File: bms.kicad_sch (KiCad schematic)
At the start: 3 parts

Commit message: buckboost: draft LM5176 4-switch power stage
Placed and wired the LM5176 (U1, HTSSOP-28-EP, LCSC C442493 per
TOPOLOGY.md) plus its support network:

Power stage: Q1..Q4 (30V/20A N-FET placeholder -- v1's FDS9926A is
undersized for v2's 5A/6.5A-peak spec, so this is marked TBD for a
proper JLCPCB Basic pick), L1 6.8uH, R8 5m current sense, boot caps
C5/C6 100nF, output caps C10/C11 22uF each.

Chip support: VIN caps C1/C2 22uF, VCC decoupling C3 2.2uF, BIAS C4
1uF, feedback R1/R2 (110k/10k -> 12.0V from LM5176's 1.0V Vref),
COMP R3 20k + C8 4.7nF, SS C7 10nF, RT R4 40.2k (~500kHz), EN
pull-up R6 100k to BAT+. MODE and DITH tied to GND.

Named nets wired: BAT+, GND, VOUT_12V, SW1, SW2, HDRV1/2, LDRV1/2,
BOOT1/2, FB, LM5176_VCC, LM5176_BIAS, SS, COMP, COMP_MID, RT, EN.
No hierarchical sheet pins -- power rails cross sheets via global
labels per the root-sheet plan.

TBD annotation on-sheet lists what needs a review pass: FET MPN,
CS/CSG hookup (currently unconnected -- either wire R8 across L1 as
high-side inductor sense OR switch to Rds(on) sensing on Q2/Q3),
SLOPE resistor R5 sizing, and optional PGOOD LED.

Also cleaned the three TEMPLATE_R/C/D placeholder symbols that
create_schematic left in all four sub-sheets.

Co-Authored-By: Claude Opus 4.7 <noreply@anthropic.com>
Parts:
- removed _TEMPLATE_C: C_TEMPLATE, symbol Device:C
- removed _TEMPLATE_D: LED_TEMPLATE, symbol Device:LED
- removed _TEMPLATE_R: R_TEMPLATE, symbol Device:R

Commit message: bms: draft the BQ76920 + cell holder + FET stack + protection sheet
27 components, 21 nets, ERC clean apart from cross-sheet BAT+/GND
globals that resolve once charger + input sheets land. Same
architecture as v1: BAT- (pre-Rsns) → R9 (5 mΩ shunt) → BQ76920
VSS+SRN + Q1(DSG).S; Q1.D + Q2.D = MID; Q2.S = system GND. Q1/Q2 are
30V/20A_NFET placeholders — pick the same MPN as the buckboost stack
when parts lock.

v2 additions vs v1: 15V TVS on VC1/VC2/VC3 cell-sense lines
(D1/D2/D3), 100nF differential cell-sense caps (v1 used 1nF —
smaller than TI EVM recommends), 5-pin I²C+ALERT breakout header.

Placement is on the sparse side (~245×155 mm sheet fill) because the
new autoplace_schematic recipe over-spreads at these compact params.
NOTES.md documents the wrap-then-restore pattern the workflow needed:
autoplace → verify the apply/rewire actually landed on disk → re-wire
by hand if not (which was the case here — apply reported success but
the file came back empty of labels/wires). Task #61 tracks the fix.

NOTES.md also captures the compact_v3 tuning + the autoplace_schematic
tool caveats so the next session doesn't retrace them.

Co-Authored-By: Claude Opus 4.7 <noreply@anthropic.com>
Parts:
- added BAT1: 3× 18650, symbol power_module_lib:BH-18650-B5BA016
- added C1, C2, C3, C4, C6: 100nF, Capacitor_SMD:C_0603_1608Metric, symbol Device:C
- added C5, C7: 1uF, Capacitor_SMD:C_0603_1608Metric, symbol Device:C
- added D1, D2, D3: SMAJ15A, Diode_SMD:D_SMA, symbol Device:D_TVS
- added J1: I2C+ALERT, Connector_PinHeader_2.54mm:PinHeader_1x05_P2.54mm_Vertical, symbol Connector_Generic:Conn_01x05
- added Q1, Q2: 30V/20A_NFET, Package_TO_SOT_SMD:SOIC-8_3.9x4.9mm_P1.27mm, symbol Device:Q_NMOS
- added R1, R10, R11, R2, R3, R4: 100, Resistor_SMD:R_0603_1608Metric, symbol Device:R
- added R5, R6, R7, R8: 10k, Resistor_SMD:R_0603_1608Metric, symbol Device:R
- added R9: 5m, Resistor_SMD:R_2512_6332Metric, symbol Device:R
- added TH1: 10k NTC (103AT), Resistor_SMD:R_0603_1608Metric, symbol Device:Thermistor_NTC
- added U1: BQ7692003, Package_SO:TSSOP-20_4.4x6.5mm_P0.65mm, symbol Battery_Management:BQ76920PW
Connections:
- new net ALERT: J1.5 (Pin_5), R7.2, U1.20 (ALERT)
- new net BAT+: BAT1.1, C6.1, R4.2, U1.10 (BAT), U1.9 (REGSRC)
- new net BAT-: BAT1.6, R1.2, R9.1, U1.18 (SRP)
- new net CAP1: C7.1, U1.7 (CAP1)
- new net CELL1_TOP: BAT1.4, BAT1.5, R2.2
- new net CELL2_TOP: BAT1.2, BAT1.3, R3.2
- new net CHG_DRV: R11.1, U1.2 (CHG)
- new net DSG_DRV: R10.1, U1.1 (DSG)
- new net GND: Q2.S
- new net MID: Q1.D, Q2.D
- new net Q1_G: Q1.G, R10.2
- new net Q2_G: Q2.G, R11.2
- new net REGOUT: C5.1, J1.1 (Pin_1), R5.1, R6.1, R7.1, R8.1, U1.8 (REGOUT)
- new net SCL: J1.4 (Pin_4), R6.2, U1.5 (SCL)
- new net SDA: J1.3 (Pin_3), R5.2, U1.4 (SDA)
- new net TS1: R8.2, TH1.1, U1.6 (TS1)
- new net VC0: C1.2, C2.1, R1.1, U1.17 (VC0)
- new net VC1: C2.2, C3.1, D1.1 (A1), R2.1, U1.16 (VC1)
- new net VC2: C3.2, C4.1, D2.1 (A1), R3.1, U1.15 (VC2)
- new net VC3: C4.2, D3.1 (A1), R4.1, U1.12 (VC5), U1.13 (VC4), U1.14 (VC3)
- new net VSS: C1.1, C5.2, C6.2, C7.2, D1.2 (A2), D2.2 (A2), D3.2 (A2), J1.2 (Pin_2), Q1.S, R9.2, TH1.2, U1.19 (SRN), U1.3 (VSS)
- no-connect marks 0 -> 1

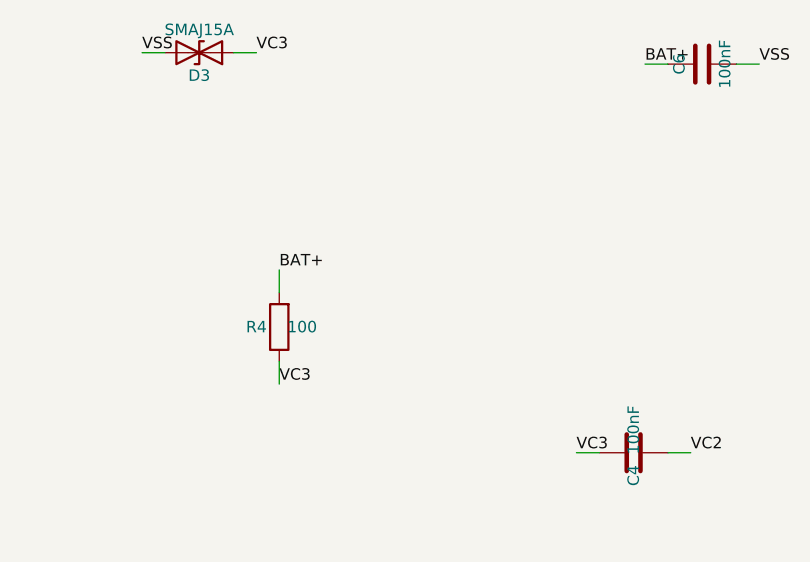
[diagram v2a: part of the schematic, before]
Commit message: input: draft USB-C + CH224K + input protection sheet; add BAT+/VBUS_9V PWR_FLAGs
input.kicad_sch (8 functional + 2 PWR_FLAG for ERC): 16-pin USB-C
receptacle (charge-only — D+/D-, SBU1/2 all NC), CH224K PD sink
controller strapped for 9V PDO via 24k CFG1→GND, SRV05-4 ESD array on
CC1/CC2, SMAJ12A TVS on VBUS_RAW, 600Ω@100MHz ferrite between VBUS_RAW
and VBUS_9V, plus 10 µF caps on both sides.

Sheet ERC clean (0 err / 2 warn, both local↔global label pairs, which
are the intentional cross-sheet plumbing).

Also added PWR_FLAG on bms.BAT+ so the cross-sheet ERC recognises the
pack rail as a driven power source.

Co-Authored-By: Claude Opus 4.7 <noreply@anthropic.com>
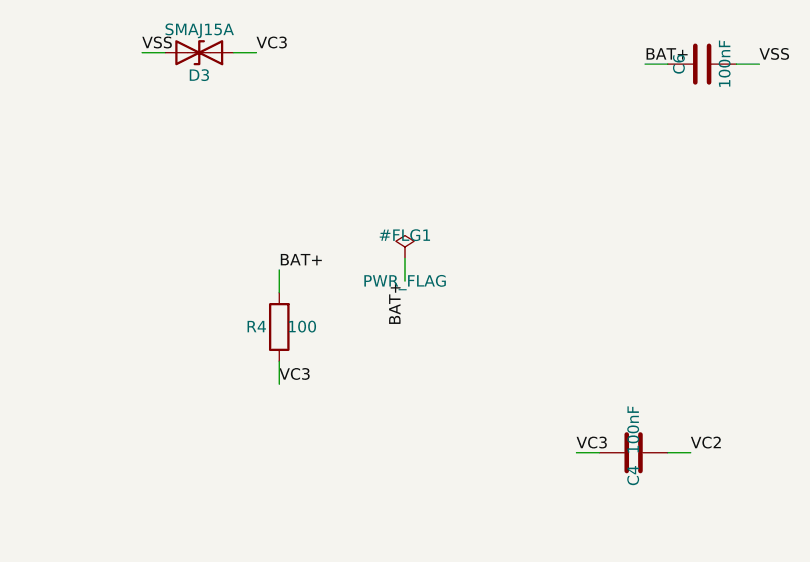
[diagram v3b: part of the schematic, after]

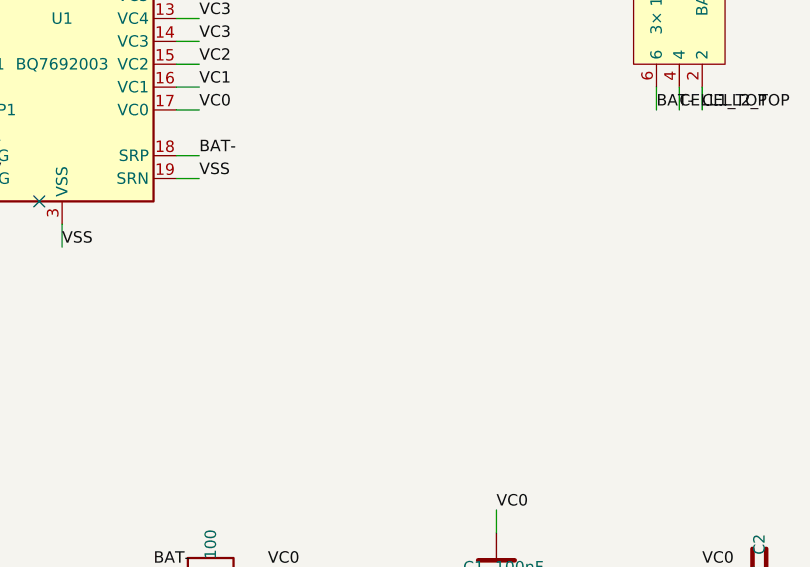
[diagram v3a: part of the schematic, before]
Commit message: buckboost: re-space at 15.24mm grid + resolve TBDs; add bms.VSS PWR_FLAG
Nuke-and-restart of buckboost.kicad_sch. The prior draft had passives
stacked at 10 mm on the same X, which silently bridged the label stubs
between rows and merged BAT+ / GND / VCC / LM5176_VCC / LM5176_BIAS /
COMP / RT into one 31-pin mega-net (feedback_schematic_vertical_spacing).
Full-project ERC caught the resulting BAT+ ↔ GND short.

Fresh layout at 15.24 mm vertical grid per column: LM5176 center, config
resistors + timing/compensation caps on the west (R6 EN / C7 SS / R4 RT
/ R5 SLOPE in col A; R3 COMP series in col B; C8 COMP cap in col C).
Power stage on the east: Q1/Q2 buck FETs, L1 6.8 µH inductor rotated 90°,
Q3/Q4 boost FETs; C1/C2 22 µF Cin at BAT+, C3/C4 LM5176 bias/vcc bypass,
C5/C6 boot caps, C10/C11 22 µF Cout at VOUT_12V, R1/R2 FB divider.

Also resolved the yesterday-TBDs from the prior buckboost commit:
- CS/CSG: use Rds(on)-of-Q2 buck-LS sensing (CS → SW1, CSG → GND). Drops
  the R8 shunt from the BOM. Cheap; loses some accuracy but keeps the
  BOM tight. Real design pass should verify against LM5176 §9.3.11 for
  buck+boost coverage.
- SLOPE: R5 = 10 kΩ to GND (placeholder — TBD per LM5176 §9.3.7 given
  final Fsw/L1 choice).
- PGOOD (U1.17): no-connect flag added.
- MODE (U1.4): tied to GND for auto PFM/PWM (efficiency-first).
- DITH (U1.5): no-connect flag added.

PWR_FLAGs: LM5176_VCC on buckboost so ERC recognises the internal LDO
as a driven power rail; bms.VSS on the BQ76920 side for the same reason.
Sheet-level ERC clean apart from cosmetic Unspecified/Passive pin-type
warnings.

Full-project ERC now: 0 errors, 34 warnings (all cosmetic — Unspecified/
Passive type mismatches, local↔global label pairs, 2 leftover Q1-Q4
'SOIC-8' footprint links from the old draft's Value fields, 1 stray
wire endpoint).

Co-Authored-By: Claude Opus 4.7 <noreply@anthropic.com>
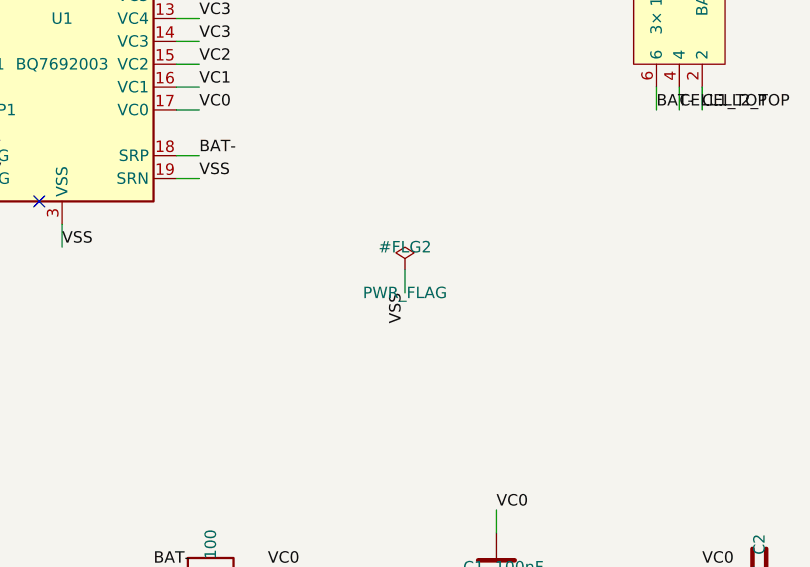
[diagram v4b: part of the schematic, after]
